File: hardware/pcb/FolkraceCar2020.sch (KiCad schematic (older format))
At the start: 74 parts, among them IC1 DRV8874PWPR, J1 Conn_01x02_Male, J2 Raspberry_Pi, J3 Conn_01x02_Male, J4 Conn Servo, J5 Conn Fan, J6 Conn Hall Effect, J7 Conn_01x06_Male, J8 Conn_01x06_Male, J9 Conn_01x06_Male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

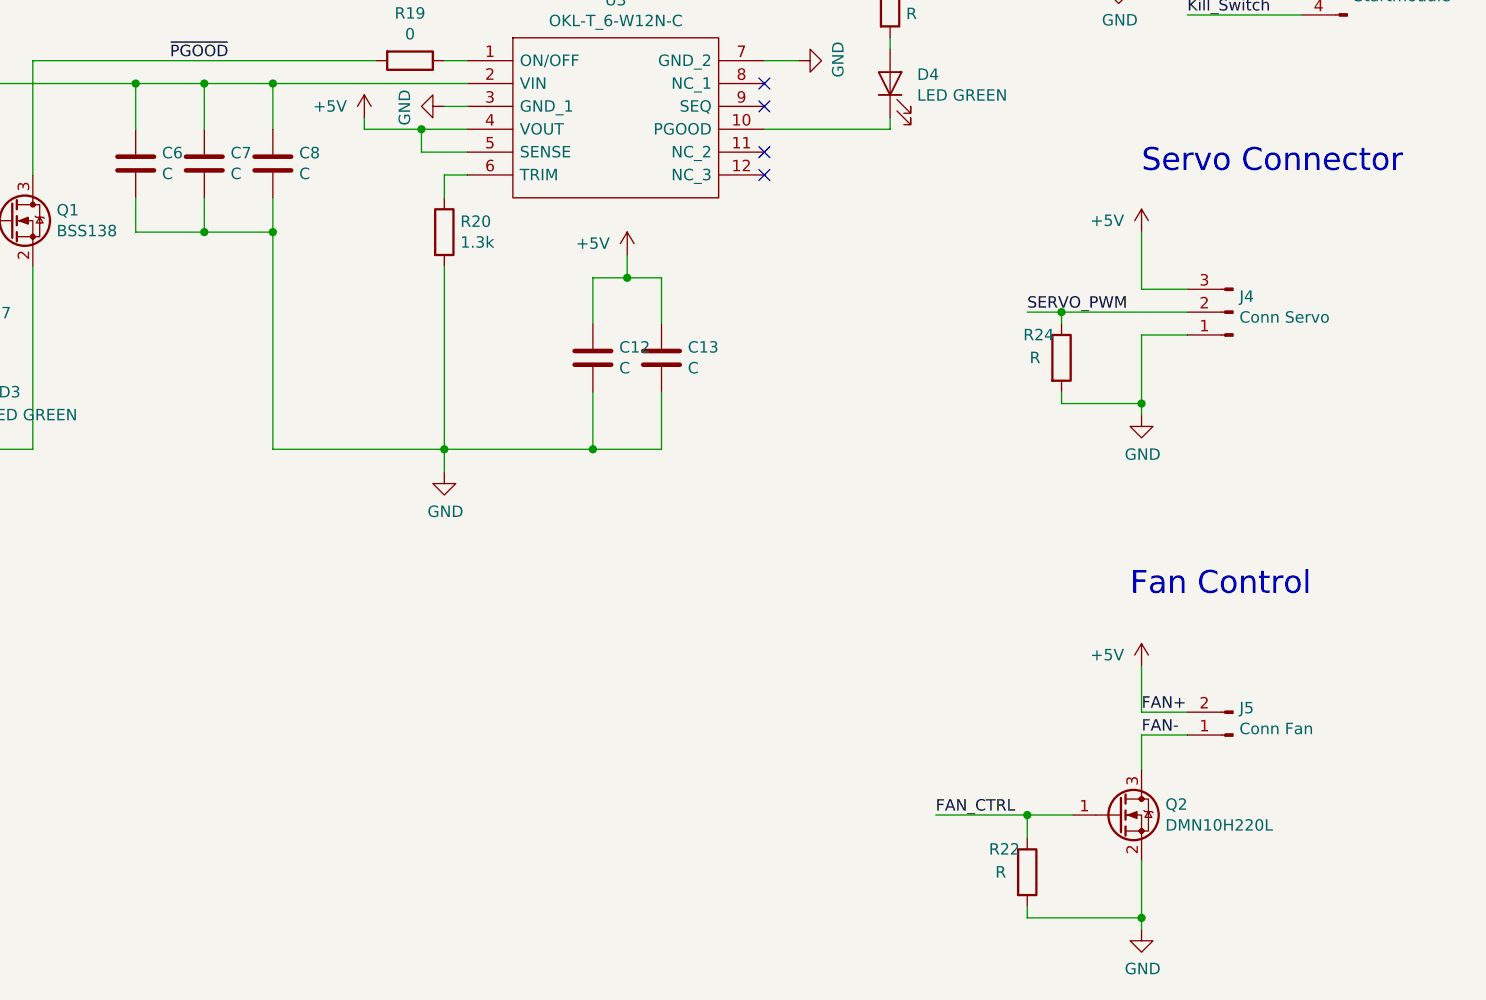
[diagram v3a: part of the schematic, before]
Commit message: updated BOM info in shcematic
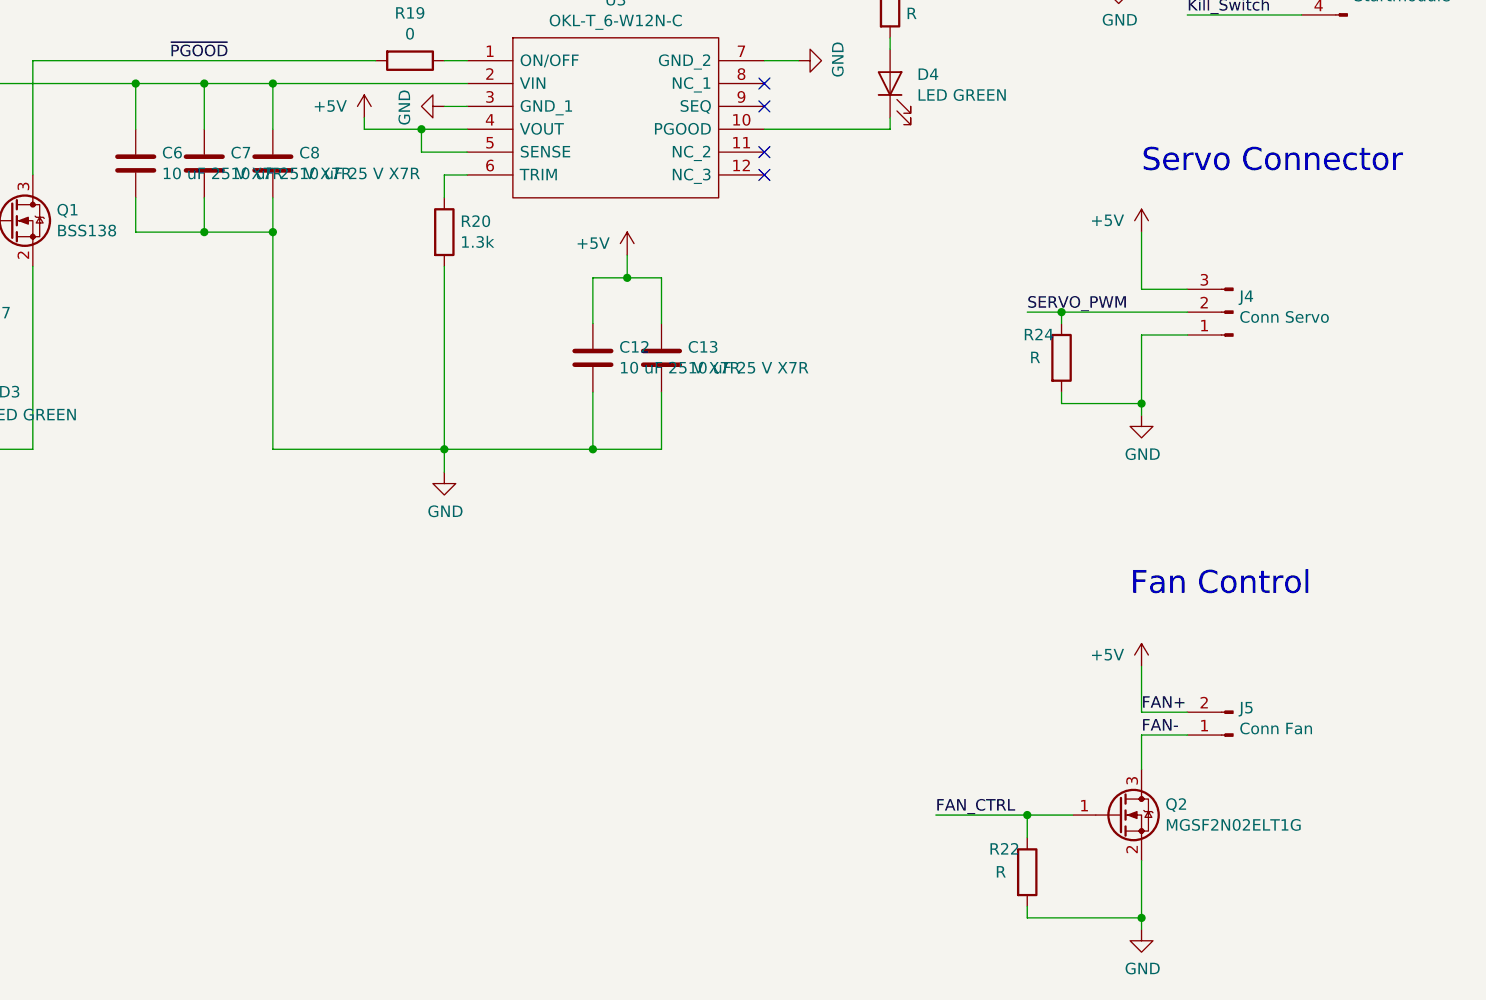
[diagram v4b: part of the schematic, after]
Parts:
- C10: DPN (none) -> 963-TMK105B7104MV-FR; Distributor (none) -> Mouser; MPN (none) -> TMK105B7104MV-FR; Manufacturer (none) -> Taiyo Yuden
- C12, C13, C6, C7, C8: value C -> 10 uF 25 V X7R; Comments (none) -> Populate if necessary; DPN (none) -> 963-TMK316AB7106KL-T; Distributor (none) -> Mouser; MPN (none) -> TMK316AB7106KL-T; Manufacturer (none) -> Taiyo Yuden
- C9: DPN (none) -> 963-TMF105B7223KVHF; Distributor (none) -> Mouser; MPN (none) -> TMF105B7223KVHF; Manufacturer (none) -> Taiyo Yuden
- IC1: DPN (none) -> 595-DRV8874PWPR; Distributor (none) -> Mouser; Height 1.2 -> (none); MPN (none) -> DRV8874PWPR; Manufacturer (none) -> Texas Instruments; Manufacturer_Name Texas Instruments -> (none); Manufacturer_Part_Number DRV8874PWPR -> (none); Mouser Part Number 595-DRV8874PWPR -> (none); Mouser Price/Stock https://www.mouser.com/Search/Refine.aspx?Keyword=595-DRV88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 -> (none)
- Q2: value DMN10H220L -> MGSF2N02ELT1G; Comments (none) -> High current, low Vgsth nmos; DPN (none) -> 863-MGSF2N02ELT1G; Distributor (none) -> Mouser; MPN (none) -> MGSF2N02ELT1G
- SW1: DPN (none) -> 653-A6S-1102-PH; Distributor PN 653-A6S-1102-PH -> (none)
- U2: Comments (none) -> Latching and automotive variant; DPN (none) -> 595-TPS25940LQRVCRQ1; Distributor (none) -> Mouser; MPN (none) -> TPS25940LQRVCRQ1; Manufacturer (none) -> Texas Instruments
- U3: DPN (none) -> 580-OKL-T/6-W12N-C; Distributor (none) -> Mouser; Height 7.2 -> (none); MPN (none) -> OKL-T_6-W12N-C; Manufacturer_Name Murata Electronics -> (none); Manufacturer_Part_Number OKL-T/6-W12N-C -> (none); Mouser Part Number 580-OKL-T/6-W12N-C -> (none); Mouser Price/Stock https://www.mouser.com/Search/Refine.aspx?Keyword=580-OKL-T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 -> (none)
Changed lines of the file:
@@
 F 3 "https://componentsearchengine.com/Datasheets/1/OKL-T_6-W12N-C.pdf" H 10250 1700 50  0001 L CNN
 F 4 "MURATA POWER SOLUTIONS - OKL-T/6-W12N-C - DC/DC CONVERTER, 30W, ADJ OUTPUT" H 10250 1600 50  0001 L CNN "Description"
-F 5 "7.2" H 10250 1500 50  0001 L CNN "Height"
-F 6 "580-OKL-T/6-W12N-C" H 10250 1400 50  0001 L CNN "Mouser Part Number"
-F 7 "https://www.mouser.com/Search/Refine.aspx?Keyword=580-OKL-T%2F6-W12N-C" H 10250 1300 50  0001 L CNN "Mouser Price/Stock"
-F 8 "Murata Electronics" H 10250 1200 50  0001 L CNN "Manufacturer_Name"
-F 9 "OKL-T/6-W12N-C" H 10250 1100 50  0001 L CNN "Manufacturer_Part_Number"
+F 5 "Mouser" H 9100 1700 50  0001 C CNN "Distributor"
+F 6 "580-OKL-T/6-W12N-C" H 9100 1700 50  0001 C CNN "DPN"
+F 7 "OKL-T_6-W12N-C" H 9100 1700 50  0001 C CNN "MPN"
 	1    9100 1700
 	1    0    0    -1
@@
 F 2 "Package_DFN_QFN:QFN-20-1EP_3x4mm_P0.5mm_EP1.65x2.65mm_ThermalVias" H 5200 3400 50  0001 C CNN
 F 3 "http://www.ti.com/lit/ds/symlink/tps25940-q1.pdf" H 5450 2050 50  0001 C CNN
+F 4 "TPS25940LQRVCRQ1" H 5200 2400 50  0001 C CNN "MPN"
+F 5 "Latching and automotive variant" H 5200 2400 50  0001 C CNN "Comments"
+F 6 "595-TPS25940LQRVCRQ1" H 5200 2400 50  0001 C CNN "DPN"
+F 7 "Mouser" H 5200 2400 50  0001 C CNN "Distributor"
+F 8 "Texas Instruments" H 5200 2400 50  0001 C CNN "Manufacturer"
 	1    5200 2400
 	1    0    0    -1
@@
 F 5 "A6S-1102-PH" H 3550 2850 50  0001 C CNN "MPN"
 F 6 "Mouser" H 3550 2850 50  0001 C CNN "Distributor"
-F 7 "653-A6S-1102-PH" H 3550 2850 50  0001 C CNN "Distributor PN"
+F 7 "653-A6S-1102-PH" H 3550 2850 50  0001 C CNN "DPN"
 	1    3550 2850
 	0    -1   -1   0
@@
 F 1 "BSS138" H 7304 2355 50  0000 L CNN
 F 2 "Package_TO_SOT_SMD:SOT-23" H 7300 2325 50  0001 L CIN
-F 3 "https://www.fairchildsemi.com/datasheets/BS/BSS138.pdf" H 7100 2400 50  0001 L CNN
+F 3 "https://www.onsemi.com/pub/Collateral/BSS138-D.PDF" H 7100 2400 50  0001 L CNN
 	1    7100 2400
 	1    0    0    -1
@@
 P 11950 5000
 F 0 "Q2" H 12154 5046 50  0000 L CNN
-F 1 "DMN10H220L" H 12154 4955 50  0000 L CNN
+F 1 "MGSF2N02ELT1G" H 12154 4955 50  0000 L CNN
 F 2 "Package_TO_SOT_SMD:SOT-23" H 12150 4925 50  0001 L CIN
-F 3 "http://www.diodes.com/assets/Datasheets/DMN10H220L.pdf" H 11950 5000 50  0001 L CNN
+F 3 "https://eu.mouser.com/datasheet/2/308/MGSF2N02EL-D-1811613.pdf" H 11950 5000 50  0001 L CNN
+F 4 "Mouser" H 11950 5000 50  0001 C CNN "Distributor"
+F 5 "863-MGSF2N02ELT1G" H 11950 5000 50  0001 C CNN "DPN"
+F 6 "MGSF2N02ELT1G" H 11950 5000 50  0001 C CNN "MPN"
+F 7 "High current, low Vgsth nmos" H 11950 5000 50  0001 C CNN "Comments"
 	1    11950 5000
 	1    0    0    -1
@@
 F 3 "https://www.ti.com/lit/gpn/DRV8874" H 7850 9050 50  0001 L CNN
 F 4 "H-Bridge Motor Driver With Integrated Current Sense and Regulation" H 7850 8950 50  0001 L CNN "Description"
-F 5 "1.2" H 7850 8850 50  0001 L CNN "Height"
-F 6 "595-DRV8874PWPR" H 7850 8750 50  0001 L CNN "Mouser Part Number"
-F 7 "https://www.mouser.com/Search/Refine.aspx?Keyword=595-DRV8874PWPR" H 7850 8650 50  0001 L CNN "Mouser Price/Stock"
-F 8 "Texas Instruments" H 7850 8550 50  0001 L CNN "Manufacturer_Name"
-F 9 "DRV8874PWPR" H 7850 8450 50  0001 L CNN "Manufacturer_Part_Number"
+F 5 "595-DRV8874PWPR" H 6600 9050 50  0001 C CNN "DPN"
+F 6 "Mouser" H 6600 9050 50  0001 C CNN "Distributor"
+F 7 "DRV8874PWPR" H 6600 9050 50  0001 C CNN "MPN"
+F 8 "Texas Instruments" H 6600 9050 50  0001 C CNN "Manufacturer"
 	1    6600 9050
 	1    0    0    -1
@@
 P 8250 2150
 F 0 "C8" H 8365 2196 50  0000 L CNN
-F 1 "C" H 8365 2105 50  0000 L CNN
+F 1 "10 uF 25 V X7R" H 8365 2105 50  0000 L CNN
 F 2 "Capacitor_SMD:C_1206_3216Metric" H 8288 2000 50  0001 C CNN
 F 3 "~" H 8250 2150 50  0001 C CNN
+F 4 "Populate if necessary" H 8250 2150 50  0001 C CNN "Comments"
+F 5 "963-TMK316AB7106KL-T" H 8250 2150 50  0001 C CNN "DPN"
+F 6 "Mouser" H 8250 2150 50  0001 C CNN "Distributor"
+F 7 "TMK316AB7106KL-T" H 8250 2150 50  0001 C CNN "MPN"
+F 8 "Taiyo Yuden" H 8250 2150 50  0001 C CNN "Manufacturer"
 	1    8250 2150
 	1    0    0    -1
@@
 F 2 "Capacitor_SMD:C_0402_1005Metric" H 8650 9250 50  0001 C CNN
 F 3 "~" H 8650 9250 50  0001 C CNN
+F 4 "Mouser" H 8650 9250 50  0001 C CNN "Distributor"
+F 5 "963-TMF105B7223KVHF" H 8650 9250 50  0001 C CNN "DPN"
+F 6 "TMF105B7223KVHF" H 8650 9250 50  0001 C CNN "MPN"
+F 7 "Taiyo Yuden" H 8650 9250 50  0001 C CNN "Manufacturer"
 	1    8650 9250
 	0    -1   -1   0
@@
 F 2 "Capacitor_SMD:C_0402_1005Metric" H 8650 9450 50  0001 C CNN
 F 3 "~" H 8650 9450 50  0001 C CNN
+F 4 "Mouser" H 8650 9450 50  0001 C CNN "Distributor"
+F 5 "963-TMK105B7104MV-FR" H 8650 9450 50  0001 C CNN "DPN"
+F 6 "TMK105B7104MV-FR" H 8650 9450 50  0001 C CNN "MPN"
+F 7 "Taiyo Yuden" H 8650 9450 50  0001 C CNN "Manufacturer"
 	1    8650 9450
 	0    -1   -1   0
@@
 P 7950 2150
 F 0 "C7" H 8065 2196 50  0000 L CNN
-F 1 "C" H 8065 2105 50  0000 L CNN
+F 1 "10 uF 25 V X7R" H 8065 2105 50  0000 L CNN
 F 2 "Capacitor_SMD:C_1206_3216Metric" H 7988 2000 50  0001 C CNN
 F 3 "~" H 7950 2150 50  0001 C CNN
+F 4 "Populate if necessary" H 7950 2150 50  0001 C CNN "Comments"
+F 5 "963-TMK316AB7106KL-T" H 7950 2150 50  0001 C CNN "DPN"
+F 6 "Mouser" H 7950 2150 50  0001 C CNN "Distributor"
+F 7 "TMK316AB7106KL-T" H 7950 2150 50  0001 C CNN "MPN"
+F 8 "Taiyo Yuden" H 7950 2150 50  0001 C CNN "Manufacturer"
 	1    7950 2150
 	1    0    0    -1
@@
 P 7650 2150
 F 0 "C6" H 7765 2196 50  0000 L CNN
-F 1 "C" H 7765 2105 50  0000 L CNN
+F 1 "10 uF 25 V X7R" H 7765 2105 50  0000 L CNN
 F 2 "Capacitor_SMD:C_1206_3216Metric" H 7688 2000 50  0001 C CNN
 F 3 "~" H 7650 2150 50  0001 C CNN
+F 4 "Populate if necessary" H 7650 2150 50  0001 C CNN "Comments"
+F 5 "963-TMK316AB7106KL-T" H 7650 2150 50  0001 C CNN "DPN"
+F 6 "Mouser" H 7650 2150 50  0001 C CNN "Distributor"
+F 7 "TMK316AB7106KL-T" H 7650 2150 50  0001 C CNN "MPN"
+F 8 "Taiyo Yuden" H 7650 2150 50  0001 C CNN "Manufacturer"
 	1    7650 2150
 	1    0    0    -1
@@
 P 9950 3000
 F 0 "C13" H 10065 3046 50  0000 L CNN
-F 1 "C" H 10065 2955 50  0000 L CNN
+F 1 "10 uF 25 V X7R" H 10065 2955 50  0000 L CNN
 F 2 "Capacitor_SMD:C_1206_3216Metric" H 9988 2850 50  0001 C CNN
 F 3 "~" H 9950 3000 50  0001 C CNN
+F 4 "Populate if necessary" H 9950 3000 50  0001 C CNN "Comments"
+F 5 "963-TMK316AB7106KL-T" H 9950 3000 50  0001 C CNN "DPN"
+F 6 "Mouser" H 9950 3000 50  0001 C CNN "Distributor"
+F 7 "TMK316AB7106KL-T" H 9950 3000 50  0001 C CNN "MPN"
+F 8 "Taiyo Yuden" H 9950 3000 50  0001 C CNN "Manufacturer"
 	1    9950 3000
 	1    0    0    -1
@@
 P 9650 3000
 F 0 "C12" H 9765 3046 50  0000 L CNN
-F 1 "C" H 9765 2955 50  0000 L CNN
+F 1 "10 uF 25 V X7R" H 9765 2955 50  0000 L CNN
 F 2 "Capacitor_SMD:C_1206_3216Metric" H 9688 2850 50  0001 C CNN
 F 3 "~" H 9650 3000 50  0001 C CNN
+F 4 "Populate if necessary" H 9650 3000 50  0001 C CNN "Comments"
+F 5 "963-TMK316AB7106KL-T" H 9650 3000 50  0001 C CNN "DPN"
+F 6 "Mouser" H 9650 3000 50  0001 C CNN "Distributor"
+F 7 "TMK316AB7106KL-T" H 9650 3000 50  0001 C CNN "MPN"
+F 8 "Taiyo Yuden" H 9650 3000 50  0001 C CNN "Manufacturer"
 	1    9650 3000
 	1    0    0    -1

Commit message: Started on BOM for Mouser order
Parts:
- SW2: DPN (none) -> 653-B3U-1000P-B; Distributor (none) -> Mouser; MPN (none) -> B3U-1000P-B
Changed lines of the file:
@@
 F 1 "SW_Push" H 5100 6244 50  0000 C CNN
 F 2 "Button_Switch_SMD:SW_SPST_B3U-1000P-B" H 5100 6250 50  0001 C CNN
-F 3 "~" H 5100 6250 50  0001 C CNN
+F 3 "https://eu.mouser.com/manufacturer/omronelectronics/" H 5100 6250 50  0001 C CNN
+F 4 "Mouser" H 5100 6050 50  0001 C CNN "Distributor"
+F 5 "653-B3U-1000P-B" H 5100 6050 50  0001 C CNN "DPN"
+F 6 "B3U-1000P-B" H 5100 6050 50  0001 C CNN "MPN"
 	1    5100 6050
 	1    0    0    -1
@@
 	1550 6550 1050 6550
 $Comp
-L power:+3.3V #PWR?
+L power:+3.3V #PWR0105
 U 1 1 5E84D9E3
 P 12400 1100
-F 0 "#PWR?" H 12400 950 50  0001 C CNN
+F 0 "#PWR0105" H 12400 950 50  0001 C CNN
 F 1 "+3.3V" H 12415 1273 50  0000 C CNN
 F 2 "" H 12400 1100 50  0001 C CNN

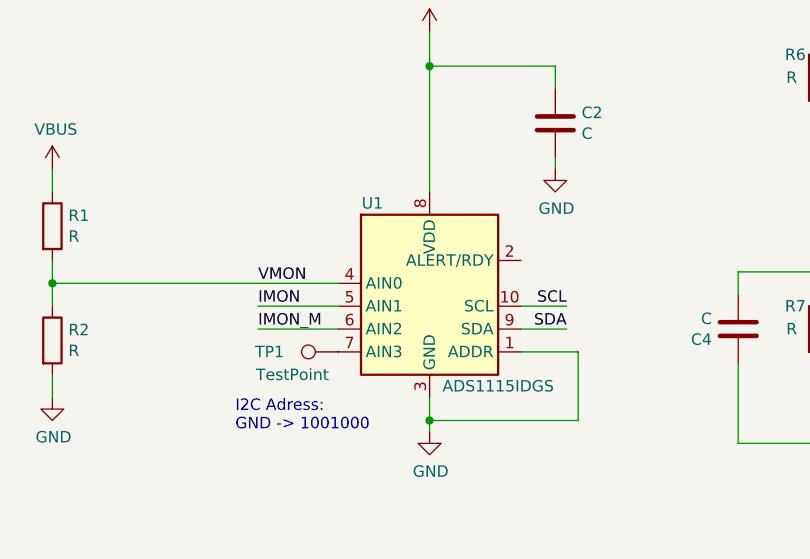
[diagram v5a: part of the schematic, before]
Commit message: Updated Mouser order list and added comment to README
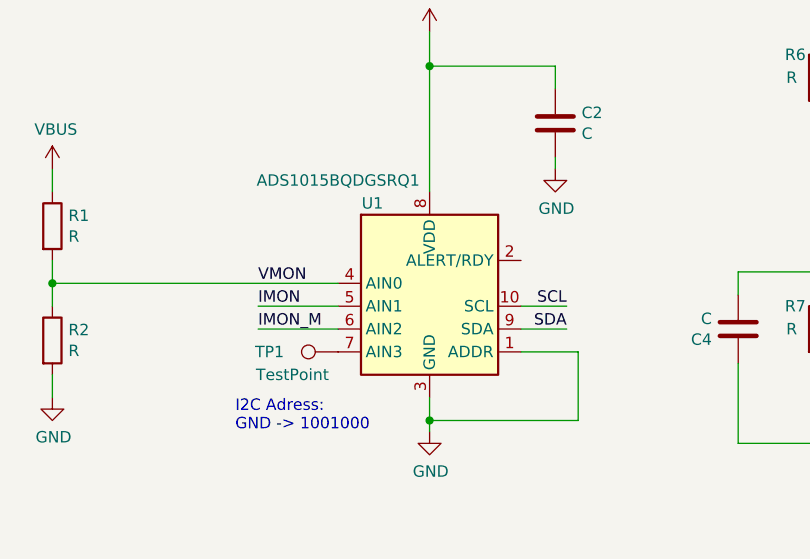
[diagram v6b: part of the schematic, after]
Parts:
- J2: Comments (none) -> Adafruit 2223 also available if there is a need for headers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; DPN (none) -> 485-2222; Distributor (none) -> Mouser; MPN (none) -> Adafruit: 2222
- U1: value ADS1115IDGS -> ADS1015BQDGSRQ1; DPN (none) -> 595-ADS1015BQDGSRQ1; Distributor (none) -> Mouser; MPN (none) -> ADS1015BQDGSRQ1
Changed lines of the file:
@@
 P 3150 9800
 F 0 "U1" H 2900 10250 50  0000 C CNN
-F 1 "ADS1115IDGS" H 3450 9450 50  0000 C CNN
+F 1 "ADS1015BQDGSRQ1" H 2750 10350 50  0000 C CNN
 F 2 "Package_SO:TSSOP-10_3x3mm_P0.5mm" H 3150 9300 50  0001 C CNN
-F 3 "http://www.ti.com/lit/ds/symlink/ads1113.pdf" H 3100 8900 50  0001 C CNN
+F 3 "http://www.ti.com/lit/ds/symlink/ads1015-q1.pdf" H 3100 8900 50  0001 C CNN
+F 4 "Mouser" H 3150 9800 50  0001 C CNN "Distributor"
+F 5 "595-ADS1015BQDGSRQ1" H 3150 9800 50  0001 C CNN "DPN"
+F 6 "ADS1015BQDGSRQ1" H 3150 9800 50  0001 C CNN "MPN"
 	1    3150 9800
 	1    0    0    -1
@@
 F 2 "Connector_PinSocket_2.54mm:PinSocket_2x20_P2.54mm_Vertical" H 2350 6050 50  0001 C CNN
 F 3 "https://www.raspberrypi.org/documentation/hardware/raspberrypi/schematics/rpi_SCH_3bplus_1p0_reduced.pdf" H 2350 6050 50  0001 C CNN
+F 4 "Mouser" H 2350 6050 50  0001 C CNN "Distributor"
+F 5 "485-2222" H 2350 6050 50  0001 C CNN "DPN"
+F 6 "Adafruit: 2222" H 2350 6050 50  0001 C CNN "MPN"
+F 7 "Adafruit 2223 also available if there is a need for headers on top" H 2350 6050 50  0001 C CNN "Comments"
 	1    2350 6050
 	1    0    0    -1
